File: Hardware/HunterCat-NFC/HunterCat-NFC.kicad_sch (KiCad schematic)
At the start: 83 parts, among them J1 Battery, P1 USB_C_Plug_USB2.0, Q1 DMG3415U-7, SW1 RESET, SW2 GPIO, SW3 GPIO1, SW4 GPIO2, SW5 ON, U1 RP2040, U2 PN7150B0HN_C11002E-PN7150B0HN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

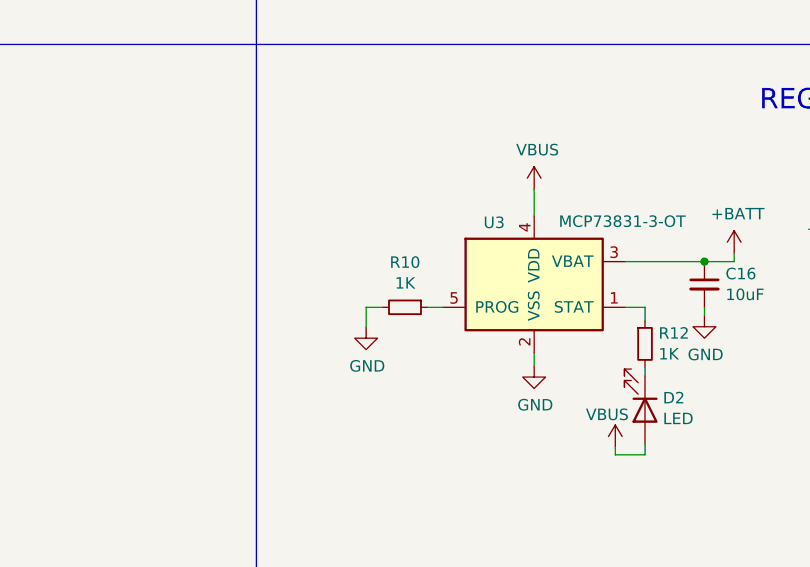
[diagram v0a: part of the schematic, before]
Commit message: change resistor charger
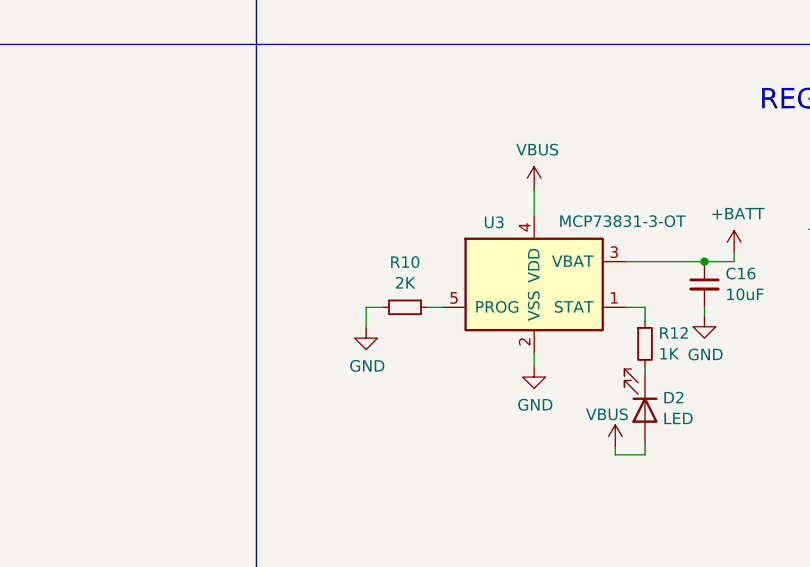
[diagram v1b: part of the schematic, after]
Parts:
- R10: value 1K -> 2K; LCSC# C517454 -> C25590; manf# CRCW08051K50FKEAC -> CRCW08052K50FKEAC
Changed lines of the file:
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@@
     (in_bom yes) (on_board yes)
     (property "Reference" "R10" (id 0) (at 262.89 137.2616 90))
-    (property "Value" "1K" (id 1) (at 262.89 139.573 90))
+    (property "Value" "2K" (id 1) (at 262.89 139.573 90))
     (property "Footprint" "Resistor_SMD:R_0603_1608Metric" (id 2) (at 262.89 142.24 0)
       (effects (font (size 1.27 1.27)) hide)
     )
-    (property "Datasheet" "~" (id 3) (at 262.89 142.24 0)
-      (effects (font (size 1.27 1.27)) hide)
-    )
-    (property "manf#" "CRCW08051K50FKEAC" (id 4) (at 262.89 142.24 0)
-      (effects (font (size 1.27 1.27)) hide)
-    )
-    (property "LCSC#" "C517454" (id 5) (at 262.89 142.24 0)
+    (property "Datasheet" "https://datasheet.lcsc.com/lcsc/2206010100_UNI-ROYAL-Uniroyal-Elec-0603WAJ0202T5E_C25590.pdf" (id 3) (at 262.89 142.24 0)
+      (effects (font (size 1.27 1.27)) hide)
+    )
+    (property "manf#" "CRCW08052K50FKEAC" (id 4) (at 262.89 142.24 0)
+      (effects (font (size 1.27 1.27)) hide)
+    )
+    (property "LCSC#" "C25590" (id 5) (at 262.89 142.24 0)
       (effects (font (size 1.27 1.27)) hide)
     )
@@
     )
     (path "/00000000-0000-0000-0000-00005e6acd31"
-      (reference "R10") (unit 1) (value "1K") (footprint "Resistor_SMD:R_0603_1608Metric")
+      (reference "R10") (unit 1) (value "2K") (footprint "Resistor_SMD:R_0603_1608Metric")
     )
     (path "/00000000-0000-0000-0000-00005e4671ec"

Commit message: Changed charge resistance to 4.7K and updated BOM
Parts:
- C1, C15: value 27pF -> (none); footprint Capacitor_SMD:C_0603_1608Metric -> (none)
- C10, C11: value 1nF/16V -> (none); footprint Capacitor_SMD:C_0603_1608Metric -> (none)
- C12, C13: value 680pF -> (none); footprint Capacitor_SMD:C_0603_1608Metric -> (none)
- C14, C18: value 100pF/50V -> (none); footprint Capacitor_SMD:C_0603_1608Metric -> (none)
- C16, C23, C24: value 10uF -> (none); footprint Capacitor_SMD:C_0603_1608Metric -> (none)
- C17, C21, C25, C26, C27, C28, C29, C30, C31, C32: value 0.1uF -> (none); footprint Capacitor_SMD:C_0603_1608Metric -> (none)
- C19, C20: value 120pF -> (none); footprint Capacitor_SMD:C_0603_1608Metric -> (none)
- C2, C22, C5, C6, C8: value 1uF -> (none); footprint Capacitor_SMD:C_0603_1608Metric -> (none)
- C3, C4: value 10pF -> (none); footprint Capacitor_SMD:C_0603_1608Metric -> (none)
- C7, C9: value 100nF -> (none); footprint Capacitor_SMD:C_0603_1608Metric -> (none)
- D1, D2, D3, D4: value LED -> (none); footprint LED_SMD:LED_0805_2012Metric_Pad1.15x1.40mm_HandSolder -> (none)
- D5: value MBR120 -> (none); footprint Diode_SMD:D_SOD-123F -> (none)
- F1: value 0.5A -> (none); footprint Fuse:Fuse_0603_1608Metric_Pad1.05x0.95mm_HandSolder -> (none)
- H1, H2, H3, H4: value MountingHole -> (none); footprint MountingHole:MountingHole_2.2mm_M2 -> (none)
- J1: value Battery -> (none); footprint Connector_PinSocket_2.54mm:PinSocket_2x01_P2.54mm_Vertical_SMD -> (none)
- JP1: value BOOT -> (none); footprint Jumper:SolderJumper-2_P1.3mm_Open_TrianglePad1.0x1.5mm -> (none)
- L1, L2: value 160nH -> (none); footprint Inductor_SMD:L_0603_1608Metric_Pad1.05x0.95mm_HandSolder -> (none)
- L3: value L -> (none); footprint hunter-cat-nfc:NFC-antenna30.4x30.4mm -> (none)
- P1: value USB_C_Plug_USB2.0 -> (none); footprint Connectors:C393939 -> (none)
- Q1: value DMG3415U-7 -> (none); footprint Package_TO_SOT_SMD:SOT-23 -> (none)
- R1, R2, R24: value 10K -> (none); footprint Resistor_SMD:R_0603_1608Metric -> (none)
- R10: value 2K -> (none); footprint Resistor_SMD:R_0603_1608Metric -> (none); LCSC# C25590 -> C116693; manf# CRCW08052K50FKEAC -> ERJ-3GEYJ472V
- R11, R13: value 2k2 -> (none); footprint Resistor_SMD:R_0603_1608Metric -> (none)
- R12, R7: value 1K -> (none); footprint Resistor_SMD:R_0603_1608Metric -> (none)
- R14, R15: value 3.24R -> (none); footprint Resistor_SMD:R_0603_1608Metric -> (none)
- R17, R18, R4: value 330 -> (none); footprint Resistor_SMD:R_0603_1608Metric -> (none)
- R19, R20, R3, R5, R6: value 100K -> (none); footprint Resistor_SMD:R_0603_1608Metric -> (none)
- R21, R22: value 27 -> (none); footprint Resistor_SMD:R_0603_1608Metric -> (none)
- R8, R9: value 5k1 -> (none); footprint Resistor_SMD:R_0603_1608Metric -> (none)
- SW1: value RESET -> (none); footprint Button_Switch_SMD:SW_SPST_TL3342 -> (none)
- SW2: value GPIO -> (none); footprint Button_Switch_SMD:SW_SPST_TL3342 -> (none)
- SW3: value GPIO1 -> (none); footprint Button_Switch_SMD:SW_SPST_TL3342 -> (none)
- SW4: value GPIO2 -> (none); footprint Button_Switch_SMD:SW_SPST_TL3342 -> (none)
- SW5: value ON -> (none); footprint hunter-cat-nfc:Micro_interruptor_SPDT -> (none)
- U1: value RP2040 -> (none); footprint RP2040:RP2040-QFN-56 -> (none)
- U2: value PN7150B0HN_C11002E-PN7150B0HN_C11002E -> (none); footprint Package_DFN_QFN:QFN-40-1EP_6x6mm_P0.5mm_EP4.6x4.6mm -> (none)
- U3: value MCP73831-3-OT -> (none); footprint Package_TO_SOT_SMD:SOT-23-5 -> (none)
- U4: value AP2112K-3.3 -> (none); footprint Package_TO_SOT_SMD:SOT-23-5 -> (none)
- U5: value W25Q16JV -> (none); footprint hunter-cat-nfc:W25Q16JVUUIQ -> (none)
- Y1: value 27.12Mhz -> (none); footprint Crystal:Crystal_SMD_2016-4Pin_2.0x1.6mm -> (none)
- Y2: value 12Mhz -> (none); footprint Crystal:Crystal_SMD_2520-4Pin_2.5x2.0mm -> (none)

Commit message: Changed Button
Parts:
- C1, C15: value (none) -> 27pF; footprint (none) -> Capacitor_SMD:C_0603_1608Metric
- C10, C11: value (none) -> 1nF/16V; footprint (none) -> Capacitor_SMD:C_0603_1608Metric
- C12, C13: value (none) -> 680pF; footprint (none) -> Capacitor_SMD:C_0603_1608Metric
- C14, C18: value (none) -> 100pF/50V; footprint (none) -> Capacitor_SMD:C_0603_1608Metric
- C16, C23, C24: value (none) -> 10uF; footprint (none) -> Capacitor_SMD:C_0603_1608Metric
- C17, C21, C25, C26, C27, C28, C29, C30, C31, C32: value (none) -> 0.1uF; footprint (none) -> Capacitor_SMD:C_0603_1608Metric
- C19, C20: value (none) -> 120pF; footprint (none) -> Capacitor_SMD:C_0603_1608Metric
- C2, C22, C5, C6, C8: value (none) -> 1uF; footprint (none) -> Capacitor_SMD:C_0603_1608Metric
- C3, C4: value (none) -> 10pF; footprint (none) -> Capacitor_SMD:C_0603_1608Metric
- C7, C9: value (none) -> 100nF; footprint (none) -> Capacitor_SMD:C_0603_1608Metric
- D1, D2, D3, D4: value (none) -> LED; footprint (none) -> LED_SMD:LED_0805_2012Metric_Pad1.15x1.40mm_HandSolder
- D5: value (none) -> MBR120; footprint (none) -> Diode_SMD:D_SOD-123F
- F1: value (none) -> 0.5A; footprint (none) -> Fuse:Fuse_0603_1608Metric_Pad1.05x0.95mm_HandSolder
- H1, H2, H3, H4: value (none) -> MountingHole; footprint (none) -> MountingHole:MountingHole_2.2mm_M2
- J1: value (none) -> Battery; footprint (none) -> Connector_PinSocket_2.54mm:PinSocket_2x01_P2.54mm_Vertical_SMD
- JP1: value (none) -> BOOT; footprint (none) -> Jumper:SolderJumper-2_P1.3mm_Open_TrianglePad1.0x1.5mm
- L1, L2: value (none) -> 160nH; footprint (none) -> Inductor_SMD:L_0603_1608Metric_Pad1.05x0.95mm_HandSolder
- L3: value (none) -> L; footprint (none) -> hunter-cat-nfc:NFC-antenna30.4x30.4mm
- P1: value (none) -> USB_C_Plug_USB2.0; footprint (none) -> Connectors:C393939
- Q1: value (none) -> DMG3415U-7; footprint (none) -> Package_TO_SOT_SMD:SOT-23
- R1, R2, R24: value (none) -> 10K; footprint (none) -> Resistor_SMD:R_0603_1608Metric
- R10: value (none) -> 4.7K; footprint (none) -> Resistor_SMD:R_0603_1608Metric
- R11, R13: value (none) -> 2k2; footprint (none) -> Resistor_SMD:R_0603_1608Metric
- R12, R7: value (none) -> 1K; footprint (none) -> Resistor_SMD:R_0603_1608Metric
- R14, R15: value (none) -> 3.24R; footprint (none) -> Resistor_SMD:R_0603_1608Metric
- R17, R18, R4: value (none) -> 330; footprint (none) -> Resistor_SMD:R_0603_1608Metric
- R19, R20, R3, R5, R6: value (none) -> 100K; footprint (none) -> Resistor_SMD:R_0603_1608Metric
- R21, R22: value (none) -> 27; footprint (none) -> Resistor_SMD:R_0603_1608Metric
- R8, R9: value (none) -> 5k1; footprint (none) -> Resistor_SMD:R_0603_1608Metric
- SW1: value (none) -> RESET; footprint (none) -> hunter-cat-nfc:KSC941JLFS; LCSC# C318890 -> C221771; manf# - -> KSC941JLFS
- SW2: value (none) -> GPIO; footprint (none) -> hunter-cat-nfc:KSC941JLFS; LCSC# C318890 -> C221771; manf# - -> KSC941JLFS
- SW3: value (none) -> GPIO1; footprint (none) -> hunter-cat-nfc:KSC941JLFS; LCSC# C318890 -> C221771; manf# - -> KSC941JLFS
- SW4: value (none) -> GPIO2; footprint (none) -> hunter-cat-nfc:KSC941JLFS; LCSC# C318890 -> C221771; manf# - -> KSC941JLFS
- SW5: value (none) -> ON; footprint (none) -> hunter-cat-nfc:Micro_interruptor_SPDT
- U1: value (none) -> RP2040; footprint (none) -> RP2040:RP2040-QFN-56
- U2: value (none) -> PN7150B0HN_C11002E-PN7150B0HN_C11002E; footprint (none) -> Package_DFN_QFN:QFN-40-1EP_6x6mm_P0.5mm_EP4.6x4.6mm
- U3: value (none) -> MCP73831-3-OT; footprint (none) -> Package_TO_SOT_SMD:SOT-23-5
- U4: value (none) -> AP2112K-3.3; footprint (none) -> Package_TO_SOT_SMD:SOT-23-5
- U5: value (none) -> W25Q16JV; footprint (none) -> hunter-cat-nfc:W25Q16JVUUIQ
- Y1: value (none) -> 27.12Mhz; footprint (none) -> Crystal:Crystal_SMD_2016-4Pin_2.0x1.6mm
- Y2: value (none) -> 12Mhz; footprint (none) -> Crystal:Crystal_SMD_2520-4Pin_2.5x2.0mm
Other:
- moved on the sheet: JP1, SW1, SW2, SW3, SW4
